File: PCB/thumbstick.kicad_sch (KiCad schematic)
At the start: 2 parts

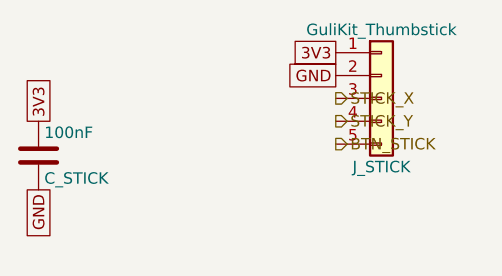
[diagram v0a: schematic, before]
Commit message: refactor: erc is clean
This gets the schematic as clean as it can be.
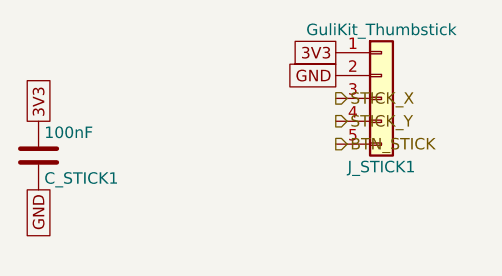
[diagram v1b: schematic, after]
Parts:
- removed C_STICK: 100nF, symbol Device:C
- removed J_STICK: GuliKit_Thumbstick, symbol Connector_Generic:Conn_01x05
- added C_STICK1: 100nF, symbol Device:C
- added J_STICK1: GuliKit_Thumbstick, symbol Connector_Generic:Conn_01x05
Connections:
- net 3V3: now also C_STICK1.1, J_STICK1.1 (Pin_1)
- net BTN_STICK: now also J_STICK1.5 (Pin_5)
- net GND: now also C_STICK1.2, J_STICK1.2 (Pin_2)
- net STICK_X: now also J_STICK1.3 (Pin_3)
- net STICK_Y: now also J_STICK1.4 (Pin_4)
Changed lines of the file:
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@@
 	(generator_version "9.0")
 	(paper "A4")
+	(global_label "GND"
+		(shape passive)
+		(at 129.54 111.76 270)
+		(fields_autoplaced yes)
+		(effects
+			(font
+				(size 1.27 1.27)
+			)
+			(justify right)
+		)
+		(property "Intersheetrefs" "${INTERSHEET_REFS}"
+			(at 129.54 111.76 0)
+			(effects
+				(font
+					(size 1.27 1.27)
+				)
+				(hide yes)
+			)
+		)
+	)
 	(global_label "3V3"
 		(shape passive)
@@
 		)
 	)
-	(global_label "GND"
-		(shape passive)
-		(at 129.54 111.76 270)
+	(global_label "3V3"
+		(shape passive)
+		(at 162.56 96.52 180)
 		(fields_autoplaced yes)
 		(effects
@@
 		)
 		(property "Intersheetrefs" "${INTERSHEET_REFS}"
-			(at 129.54 111.76 0)
-			(effects
-				(font
-					(size 1.27 1.27)
-				)
-				(hide yes)
-			)
-		)
-	)
-	(global_label "3V3"
-		(shape passive)
-		(at 162.56 96.52 180)
-		(fields_autoplaced yes)
-		(effects
-			(font
-				(size 1.27 1.27)
-			)
-			(justify right)
-		)
-		(property "Intersheetrefs" "${INTERSHEET_REFS}"
 			(at 162.56 96.52 0)
 			(effects
@@
 				(hide yes)
 			)
+		)
+	)
+	(hierarchical_label "STICK_X"
+		(shape output)
+		(at 162.56 101.6 0)
+		(effects
+			(font
+				(size 1.27 1.27)
+			)
+			(justify left)
 		)
 	)
@@
 		)
 	)
-	(hierarchical_label "STICK_X"
-		(shape output)
-		(at 162.56 101.6 0)
-		(effects
-			(font
-				(size 1.27 1.27)
-			)
-			(justify left)
-		)
-	)
 	(hierarchical_label "BTN_STICK"
 		(shape output)
@@
 			)
 			(justify left)
+		)
+	)
+	(symbol
+		(lib_id "Connector_Generic:Conn_01x05")
+		(at 167.64 101.6 0)
+		(unit 1)
+		(exclude_from_sim no)
+		(in_bom yes)
+		(on_board yes)
+		(dnp no)
+		(fields_autoplaced yes)
+		(property "Reference" "J_STICK1"
+			(at 167.64 109.22 0)
+			(effects
+				(font
+					(size 1.27 1.27)
+				)
+			)
+		)
+		(property "Value" "GuliKit_Thumbstick"
+			(at 167.64 93.98 0)
+			(effects
+				(font
+					(size 1.27 1.27)
+				)
+			)
+		)
+		(property "Footprint" ""
+			(at 167.64 101.6 0)
+			(effects
+				(font
+					(size 1.27 1.27)
+				)
+				(hide yes)
+			)
+		)
+		(property "Datasheet" "~"
+			(at 167.64 101.6 0)
+			(effects
+				(font
+					(size 1.27 1.27)
+				)
+				(hide yes)
+			)
+		)
+		(property "Description" "Generic connector, single row, 01x05, script generated (kicad-library-utils/schlib/autogen/connector/)"
+			(at 167.64 101.6 0)
+			(effects
+				(font
+					(size 1.27 1.27)
+				)
+				(hide yes)
+			)
+		)
+		(pin "1"
+		)
+		(pin "2"
+		)
+		(pin "3"
+		)
+		(pin "4"
+		)
+		(pin "5"
+		)
+		(instances
+			(project "snips_controller"
+				(path "/70589bdd-acbd-4920-8e78-aa58d10832b9/bfb4bb8d-7e51-441a-9c52-8d66824f53e1"
+					(reference "J_STICK1")
+					(unit 1)
+				)
+			)
 		)
 	)
@@
 		(dnp no)
 		(fields_autoplaced yes)
-		(property "Reference" "C_STICK"
+		(property "Reference" "C_STICK1"
 			(at 130.175 110.49 0)
 			(effects
@@
 		(instances
 			(project "snips_controller"
-				(path "/2289c08f-f540-4e27-86fd-a28b71d1d149/b18b6387-74fa-49ca-90a7-3b13e5aeea3c"
-					(reference "C_STICK")
+				(path "/70589bdd-acbd-4920-8e78-aa58d10832b9/bfb4bb8d-7e51-441a-9c52-8d66824f53e1"
+					(reference "C_STICK1")
 					(unit 1)
 				)
-			)
-		)
-	)
-	(symbol
-		(lib_id "Connector_Generic:Conn_01x05")
-		(at 167.64 101.6 0)
-		(unit 1)
-		(exclude_from_sim no)
-		(in_bom yes)
-		(on_board yes)
-		(dnp no)
-		(fields_autoplaced yes)
-		(property "Reference" "J_STICK"
-			(at 167.64 109.22 0)
-			(effects
-				(font
-					(size 1.27 1.27)
-				)
-			)
-		)
-		(property "Value" "GuliKit_Thumbstick"
-			(at 167.64 93.98 0)
-			(effects
-				(font
-					(size 1.27 1.27)
-				)
-			)
-		)
-		(property "Footprint" ""
-			(at 167.64 101.6 0)
-			(effects
-				(font
-					(size 1.27 1.27)
-				)
-				(hide yes)
-			)
-		)
-		(property "Datasheet" "~"
-			(at 167.64 101.6 0)
-			(effects
-				(font
-					(size 1.27 1.27)
-				)
-				(hide yes)
-			)
-		)
-		(property "Description" "Generic connector, single row, 01x05, script generated (kicad-library-utils/schlib/autogen/connector/)"
-			(at 167.64 101.6 0)
-			(effects
-				(font
-					(size 1.27 1.27)
-				)
-				(hide yes)
-			)
-		)
-		(pin "1"
-		)
-		(pin "2"
-		)
-		(pin "3"
-		)
-		(pin "4"
-		)
-		(pin "5"
-		)
-		(instances
-			(project "snips_controller"
-				(path "/2289c08f-f540-4e27-86fd-a28b71d1d149/b18b6387-74fa-49ca-90a7-3b13e5aeea3c"
-					(reference "J_STICK")
-					(unit 1)
-				)

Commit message: refactor: switch over to esp32-s3-wroom1 (#13)
This refactors to the esp32-s3 to avoid every problem we encountered with the raspberry pi options.
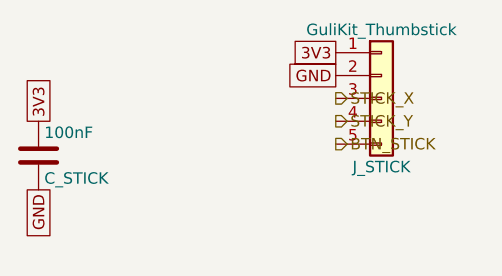
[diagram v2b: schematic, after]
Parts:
- removed C_STICK1: 100nF, symbol Device:C
- removed J_STICK1: GuliKit_Thumbstick, symbol Connector_Generic:Conn_01x05
- added C_STICK: 100nF, Capacitor_SMD:C_0402_1005Metric, symbol Device:C
- added J_STICK: GuliKit_Thumbstick, Connector_PinHeader_2.54mm:PinHeader_1x05_P2.54mm_Vertical, symbol Connector_Generic:Conn_01x05
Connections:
- net 3V3: now also C_STICK.1, J_STICK.1 (Pin_1)
- net BTN_STICK: now also J_STICK.5 (Pin_5)
- net GND: now also C_STICK.2, J_STICK.2 (Pin_2)
- net STICK_X: now also J_STICK.3 (Pin_3)
- net STICK_Y: now also J_STICK.4 (Pin_4)
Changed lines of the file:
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@@
 (kicad_sch
 	(version 20250114)
-	(generator "eeschema")
-	(generator_version "9.0")
+	(generator "kicaddy")
+	(generator_version "0.1.0")
 	(paper "A4")
-	(global_label "GND"
+	(global_label "3V3"
 		(shape passive)
-		(at 129.54 111.76 270)
+		(at 162.56 96.52 0)
 		(fields_autoplaced yes)
-		(effects
-			(font
-				(size 1.27 1.27)
-			)
-			(justify right)
-		)
-		(property "Intersheetrefs" "${INTERSHEET_REFS}"
-			(at 129.54 111.76 0)
-			(effects
-				(font
-					(size 1.27 1.27)
-				)
-				(hide yes)
-			)
-		)
+		(effects (font (size 1.27 1.27)) (justify right))
 	)
 	(global_label "3V3"
 		(shape passive)
-		(at 129.54 104.14 90)
+		(at 129.54 104.14 270)
 		(fields_autoplaced yes)
-		(effects
-			(font
-				(size 1.27 1.27)
-			)
-			(justify left)
-		)
-		(property "Intersheetrefs" "${INTERSHEET_REFS}"
-			(at 129.54 104.14 0)
-			(effects
-				(font
-					(size 1.27 1.27)
-				)
-				(hide yes)
-			)
-		)
+		(effects (font (size 1.27 1.27)) (justify left))
 	)
 	(global_label "GND"
 		(shape passive)
-		(at 162.56 99.06 180)
+		(at 162.56 99.06 0)
 		(fields_autoplaced yes)
-		(effects
-			(font
-				(size 1.27 1.27)
-			)
-			(justify right)
-		)
-		(property "Intersheetrefs" "${INTERSHEET_REFS}"
-			(at 162.56 99.06 0)
-			(effects
-				(font
-					(size 1.27 1.27)
-				)
-				(hide yes)
-			)
-		)
+		(effects (font (size 1.27 1.27)) (justify right))
 	)
-	(global_label "3V3"
+	(global_label "GND"
 		(shape passive)
-		(at 162.56 96.52 180)
+		(at 129.54 111.76 90)
 		(fields_autoplaced yes)
-		(effects
-			(font
-				(size 1.27 1.27)
-			)
-			(justify right)
-		)
-		(property "Intersheetrefs" "${INTERSHEET_REFS}"
-			(at 162.56 96.52 0)
-			(effects
-				(font
-					(size 1.27 1.27)
-				)
-				(hide yes)
-			)
-		)
+		(effects (font (size 1.27 1.27)) (justify right))
 	)
 	(hierarchical_label "STICK_X"
 		(shape output)
 		(at 162.56 101.6 0)
-		(effects
-			(font
-				(size 1.27 1.27)
-			)
-			(justify left)
-		)
 	)
 	(hierarchical_label "STICK_Y"
 		(shape output)
 		(at 162.56 104.14 0)
-		(effects
-			(font
-				(size 1.27 1.27)
-			)
-			(justify left)
-		)
 	)
 	(hierarchical_label "BTN_STICK"
 		(shape output)
 		(at 162.56 106.68 0)
-		(effects
-			(font
-				(size 1.27 1.27)
+	)
+	(symbol
+		(lib_id "Device:C")
+		(at 129.54 107.95 0)
+		(unit 1)
+		(exclude_from_sim no)
+		(in_bom yes)
+		(on_board yes)
+		(dnp no)
+		(fields_autoplaced yes)
+		(property "Reference"
+			"C_STICK"
+			(at 130.175 110.49 0)
+			(effects (font (size 1.27 1.27)) (justify left))
+		)
+		(property "Value"
+			"100nF"
+			(at 130.175 105.41 0)
+			(effects (font (size 1.27 1.27)) (justify left))
+		)
+		(property "Footprint"
+			"Capacitor_SMD:C_0402_1005Metric"
+			(at 130.5052 104.14 0)
+			(effects (font (size 1.27 1.27)) (hide yes))
+		)
+		(property "Datasheet"
+			"~"
+			(at 129.54 107.95 0)
+			(effects (font (size 1.27 1.27)) (hide yes))
+		)
+		(property "Description"
+			"Unpolarized capacitor"
+			(at 129.54 107.95 0)
+			(effects (font (size 1.27 1.27)) (hide yes))
+		)
+		(pin "1")
+		(pin "2")
+		(instances
+			(project ""
+				(path "/868f8289-8434-4465-b2f4-2accc5e40bab/7a3e413b-2e94-4a8b-a1cc-2db3e975d99a"
+					(reference "C_STICK")
+					(unit 1)
+				)
 			)
-			(justify left)
 		)
 	)
@@
 		(dnp no)
 		(fields_autoplaced yes)
-		(property "Reference" "J_STICK1"
+		(property "Reference"
+			"J_STICK"
 			(at 167.64 109.22 0)
-			(effects
-				(font
-					(size 1.27 1.27)
-				)
-			)
+			(effects (font (size 1.27 1.27)))
 		)
-		(property "Value" "GuliKit_Thumbstick"
+		(property "Value"
+			"GuliKit_Thumbstick"
 			(at 167.64 93.98 0)
-			(effects
-				(font
-					(size 1.27 1.27)
-				)
-			)
+			(effects (font (size 1.27 1.27)))
 		)
-		(property "Footprint" ""
+		(property "Footprint"
+			"Connector_PinHeader_2.54mm:PinHeader_1x05_P2.54mm_Vertical"
 			(at 167.64 101.6 0)
-			(effects
-				(font
-					(size 1.27 1.27)
-				)
-				(hide yes)
-			)
+			(effects (font (size 1.27 1.27)) (hide yes))
 		)
-		(property "Datasheet" "~"
+		(property "Datasheet"
+			"~"
 			(at 167.64 101.6 0)
-			(effects
-				(font
-					(size 1.27 1.27)
-				)
-				(hide yes)
-			)
+			(effects (font (size 1.27 1.27)) (hide yes))
 		)
-		(property "Description" "Generic connector, single row, 01x05, script generated (kicad-library-utils/schlib/autogen/connector/)"
+		(property "Description"
+			"Generic connector, single row, 01x05, script generated (kicad-library-utils/schlib/autogen/connector/)"
 			(at 167.64 101.6 0)
-			(effects
-				(font
-					(size 1.27 1.27)
-				)
-				(hide yes)
-			)
+			(effects (font (size 1.27 1.27)) (hide yes))
 		)
-		(pin "1"
-		)
-		(pin "2"
-		)
-		(pin "3"
-		)
-		(pin "4"
-		)
-		(pin "5"
-		)
+		(pin "1")
+		(pin "2")
+		(pin "3")
+		(pin "4")
+		(pin "5")
 		(instances
-			(project "snips_controller"
-				(path "/70589bdd-acbd-4920-8e78-aa58d10832b9/bfb4bb8d-7e51-441a-9c52-8d66824f53e1"
-					(reference "J_STICK1")
+			(project ""
+				(path "/868f8289-8434-4465-b2f4-2accc5e40bab/7a3e413b-2e94-4a8b-a1cc-2db3e975d99a"
+					(reference "J_STICK")
 					(unit 1)
 				)
@@
 		)
 	)
-	(symbol
-		(lib_id "Device:C")
-		(at 129.54 107.95 0)
-		(unit 1)
-		(exclude_from_sim no)
-		(in_bom yes)
-		(on_board yes)
-		(dnp no)
-		(fields_autoplaced yes)
-		(property "Reference" "C_STICK1"
-			(at 130.175 110.49 0)
-			(effects
-				(font
-					(size 1.27 1.27)
-				)
-				(justify left)
-			)
-		)
-		(property "Value" "100nF"
-			(at 130.175 105.41 0)
-			(effects
-				(font
-					(size 1.27 1.27)
-				)
-				(justify left)
-			)
-		)
-		(property "Footprint" ""
-			(at 130.5052 104.14 0)
-			(effects
-				(font
-					(size 1.27 1.27)
-				)
-				(hide yes)
-			)
-		)
-		(property "Datasheet" "~"
-			(at 129.54 107.95 0)
-			(effects
-				(font
-					(size 1.27 1.27)
-				)
-				(hide yes)
-			)
-		)
-		(property "Description" "Unpolarized capacitor"
-			(at 129.54 107.95 0)
-			(effects
-				(font
-					(size 1.27 1.27)
-				)
-				(hide yes)
-			)
-		)
-		(pin "1"
-		)
-		(pin "2"
-		)
-		(instances
-			(project "snips_controller"
-				(path "/70589bdd-acbd-4920-8e78-aa58d10832b9/bfb4bb8d-7e51-441a-9c52-8d66824f53e1"
-					(reference "C_STICK1")
-					(unit 1)
-				)
-			)
+	(sheet_instances
+		(path "/868f8289-8434-4465-b2f4-2accc5e40bab/7a3e413b-2e94-4a8b-a1cc-2db3e975d99a"
+			(page "1")
 		)
 	)
+	(embedded_fonts no)
 )

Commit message: cleanup: annotations and library updates
This is just a task to update the kicad libraries and annotations internally to get that clean ERC.
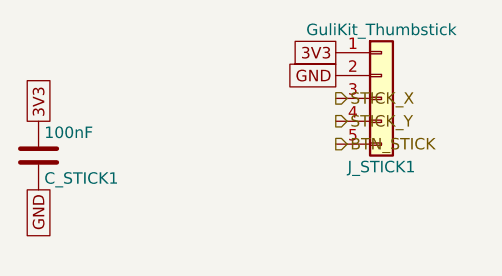
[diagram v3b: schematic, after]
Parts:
- renumbered C_STICK to C_STICK1, J_STICK to J_STICK1
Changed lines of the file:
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@@
 (kicad_sch
 	(version 20250114)
-	(generator "kicaddy")
-	(generator_version "0.1.0")
+	(generator "eeschema")
+	(generator_version "9.0")
 	(paper "A4")
+	(global_label "GND"
+		(shape passive)
+		(at 129.54 111.76 270)
+		(fields_autoplaced yes)
+		(effects
+			(font
+				(size 1.27 1.27)
+			)
+			(justify right)
+		)
+		(property "Intersheetrefs" "${INTERSHEET_REFS}"
+			(at 129.54 111.76 0)
+			(effects
+				(font
+					(size 1.27 1.27)
+				)
+				(hide yes)
+			)
+		)
+	)
 	(global_label "3V3"
 		(shape passive)
-		(at 162.56 96.52 0)
-		(fields_autoplaced yes)
-		(effects (font (size 1.27 1.27)) (justify right))
+		(at 162.56 96.52 180)
+		(fields_autoplaced yes)
+		(effects
+			(font
+				(size 1.27 1.27)
+			)
+			(justify right)
+		)
+		(property "Intersheetrefs" "${INTERSHEET_REFS}"
+			(at 162.56 96.52 0)
+			(effects
+				(font
+					(size 1.27 1.27)
+				)
+				(hide yes)
+			)
+		)
 	)
 	(global_label "3V3"
 		(shape passive)
-		(at 129.54 104.14 270)
-		(fields_autoplaced yes)
-		(effects (font (size 1.27 1.27)) (justify left))
+		(at 129.54 104.14 90)
+		(fields_autoplaced yes)
+		(effects
+			(font
+				(size 1.27 1.27)
+			)
+			(justify left)
+		)
+		(property "Intersheetrefs" "${INTERSHEET_REFS}"
+			(at 129.54 104.14 0)
+			(effects
+				(font
+					(size 1.27 1.27)
+				)
+				(hide yes)
+			)
+		)
 	)
 	(global_label "GND"
 		(shape passive)
-		(at 162.56 99.06 0)
-		(fields_autoplaced yes)
-		(effects (font (size 1.27 1.27)) (justify right))
-	)
-	(global_label "GND"
-		(shape passive)
-		(at 129.54 111.76 90)
-		(fields_autoplaced yes)
-		(effects (font (size 1.27 1.27)) (justify right))
+		(at 162.56 99.06 180)
+		(fields_autoplaced yes)
+		(effects
+			(font
+				(size 1.27 1.27)
+			)
+			(justify right)
+		)
+		(property "Intersheetrefs" "${INTERSHEET_REFS}"
+			(at 162.56 99.06 0)
+			(effects
+				(font
+					(size 1.27 1.27)
+				)
+				(hide yes)
+			)
+		)
 	)
 	(hierarchical_label "STICK_X"
 		(shape output)
 		(at 162.56 101.6 0)
+		(effects
+			(font
+				(size 1.27 1.27)
+			)
+			(justify left)
+		)
+	)
+	(hierarchical_label "BTN_STICK"
+		(shape output)
+		(at 162.56 106.68 0)
+		(effects
+			(font
+				(size 1.27 1.27)
+			)
+			(justify left)
+		)
 	)
 	(hierarchical_label "STICK_Y"
 		(shape output)
 		(at 162.56 104.14 0)
-	)
-	(hierarchical_label "BTN_STICK"
-		(shape output)
-		(at 162.56 106.68 0)
+		(effects
+			(font
+				(size 1.27 1.27)
+			)
+			(justify left)
+		)
+	)
+	(symbol
+		(lib_id "Connector_Generic:Conn_01x05")
+		(at 167.64 101.6 0)
+		(unit 1)
+		(exclude_from_sim no)
+		(in_bom yes)
+		(on_board yes)
+		(dnp no)
+		(fields_autoplaced yes)
+		(property "Reference" "J_STICK1"
+			(at 167.64 109.22 0)
+			(effects
+				(font
+					(size 1.27 1.27)
+				)
+			)
+		)
+		(property "Value" "GuliKit_Thumbstick"
+			(at 167.64 93.98 0)
+			(effects
+				(font
+					(size 1.27 1.27)
+				)
+			)
+		)
+		(property "Footprint" "Connector_PinHeader_2.54mm:PinHeader_1x05_P2.54mm_Vertical"
+			(at 167.64 101.6 0)
+			(effects
+				(font
+					(size 1.27 1.27)
+				)
+				(hide yes)
+			)
+		)
+		(property "Datasheet" "~"
+			(at 167.64 101.6 0)
+			(effects
+				(font
+					(size 1.27 1.27)
+				)
+				(hide yes)
+			)
+		)
+		(property "Description" "Generic connector, single row, 01x05, script generated (kicad-library-utils/schlib/autogen/connector/)"
+			(at 167.64 101.6 0)
+			(effects
+				(font
+					(size 1.27 1.27)
+				)
+				(hide yes)
+			)
+		)
+		(pin "1"
+		)
+		(pin "2"
+		)
+		(pin "3"
+		)
+		(pin "4"
+		)
+		(pin "5"
+		)
+		(instances
+			(project "snips_controller"
+				(path "/868f8289-8434-4465-b2f4-2accc5e40bab/7a3e413b-2e94-4a8b-a1cc-2db3e975d99a"
+					(reference "J_STICK1")
+					(unit 1)
+				)
+			)
+		)
 	)
 	(symbol
@@
 		(dnp no)
 		(fields_autoplaced yes)
-		(property "Reference"
-			"C_STICK"
+		(property "Reference" "C_STICK1"
 			(at 130.175 110.49 0)
-			(effects (font (size 1.27 1.27)) (justify left))
-		)
-		(property "Value"
-			"100nF"
+			(effects
+				(font
+					(size 1.27 1.27)
+				)
+				(justify left)
+			)
+		)
+		(property "Value" "100nF"
 			(at 130.175 105.41 0)
-			(effects (font (size 1.27 1.27)) (justify left))
-		)
-		(property "Footprint"
-			"Capacitor_SMD:C_0402_1005Metric"
+			(effects
+				(font
+					(size 1.27 1.27)
+				)
+				(justify left)
+			)
+		)
+		(property "Footprint" "Capacitor_SMD:C_0402_1005Metric"
 			(at 130.5052 104.14 0)
-			(effects (font (size 1.27 1.27)) (hide yes))
-		)
-		(property "Datasheet"
-			"~"
+			(effects
+				(font
+					(size 1.27 1.27)
+				)
+				(hide yes)
+			)
+		)
+		(property "Datasheet" "~"
 			(at 129.54 107.95 0)
-			(effects (font (size 1.27 1.27)) (hide yes))
-		)
-		(property "Description"
-			"Unpolarized capacitor"
+			(effects
+				(font
+					(size 1.27 1.27)
+				)
+				(hide yes)
+			)
+		)
+		(property "Description" "Unpolarized capacitor"
 			(at 129.54 107.95 0)
-			(effects (font (size 1.27 1.27)) (hide yes))
-		)
-		(pin "1")
-		(pin "2")
+			(effects
+				(font
+					(size 1.27 1.27)
+				)
+				(hide yes)
+			)
+		)
+		(pin "1"
+		)
+		(pin "2"
+		)
 		(instances
-			(project ""
+			(project "snips_controller"
 				(path "/868f8289-8434-4465-b2f4-2accc5e40bab/7a3e413b-2e94-4a8b-a1cc-2db3e975d99a"
-					(reference "C_STICK")
+					(reference "C_STICK1")
 					(unit 1)
 				)
@@
 		)
 	)
-	(symbol
-		(lib_id "Connector_Generic:Conn_01x05")
-		(at 167.64 101.6 0)
-		(unit 1)
-		(exclude_from_sim no)
-		(in_bom yes)
-		(on_board yes)
-		(dnp no)
-		(fields_autoplaced yes)
-		(property "Reference"
-			"J_STICK"
-			(at 167.64 109.22 0)
-			(effects (font (size 1.27 1.27)))
-		)
-		(property "Value"
-			"GuliKit_Thumbstick"
-			(at 167.64 93.98 0)
-			(effects (font (size 1.27 1.27)))
-		)
-		(property "Footprint"
-			"Connector_PinHeader_2.54mm:PinHeader_1x05_P2.54mm_Vertical"
-			(at 167.64 101.6 0)
-			(effects (font (size 1.27 1.27)) (hide yes))
-		)
-		(property "Datasheet"
-			"~"
-			(at 167.64 101.6 0)
-			(effects (font (size 1.27 1.27)) (hide yes))
-		)
-		(property "Description"
-			"Generic connector, single row, 01x05, script generated (kicad-library-utils/schlib/autogen/connector/)"
-			(at 167.64 101.6 0)
-			(effects (font (size 1.27 1.27)) (hide yes))
-		)
-		(pin "1")
-		(pin "2")
-		(pin "3")
-		(pin "4")
-		(pin "5")
-		(instances
-			(project ""
-				(path "/868f8289-8434-4465-b2f4-2accc5e40bab/7a3e413b-2e94-4a8b-a1cc-2db3e975d99a"
-					(reference "J_STICK")
-					(unit 1)
-				)
-			)
-		)
-	)
-	(sheet_instances
-		(path "/868f8289-8434-4465-b2f4-2accc5e40bab/7a3e413b-2e94-4a8b-a1cc-2db3e975d99a"
-			(page "1")
-		)
-	)
-	(embedded_fonts no)
 )
